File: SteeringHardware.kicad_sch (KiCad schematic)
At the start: 59 parts, among them J1 Conn_ARM_JTAG_SWD_10, J10 Output, J11 Input, J12 Output, J13 Input, J14 Input, J15 Output, J16 Input, J17 Output, J18 Output, J19 Input, J2 USB_B_Micro, J20 Input, J3 Conn_01x09_Female, J4 Output, J5 Input, J6 Input, J7 Output, J8 Input, J9 Input, Q1 AO3400A, Q2 AO3400A, Q3 AO3400A, Q4 AO3400A, Q5 AO3400A, Q6 AO3400A, Q7 AO3400A, U1 STM32F072RBTx, U3 TPS2113, U4 TCAN1042xV, U6 TPS5430DDA, U7 HY28B

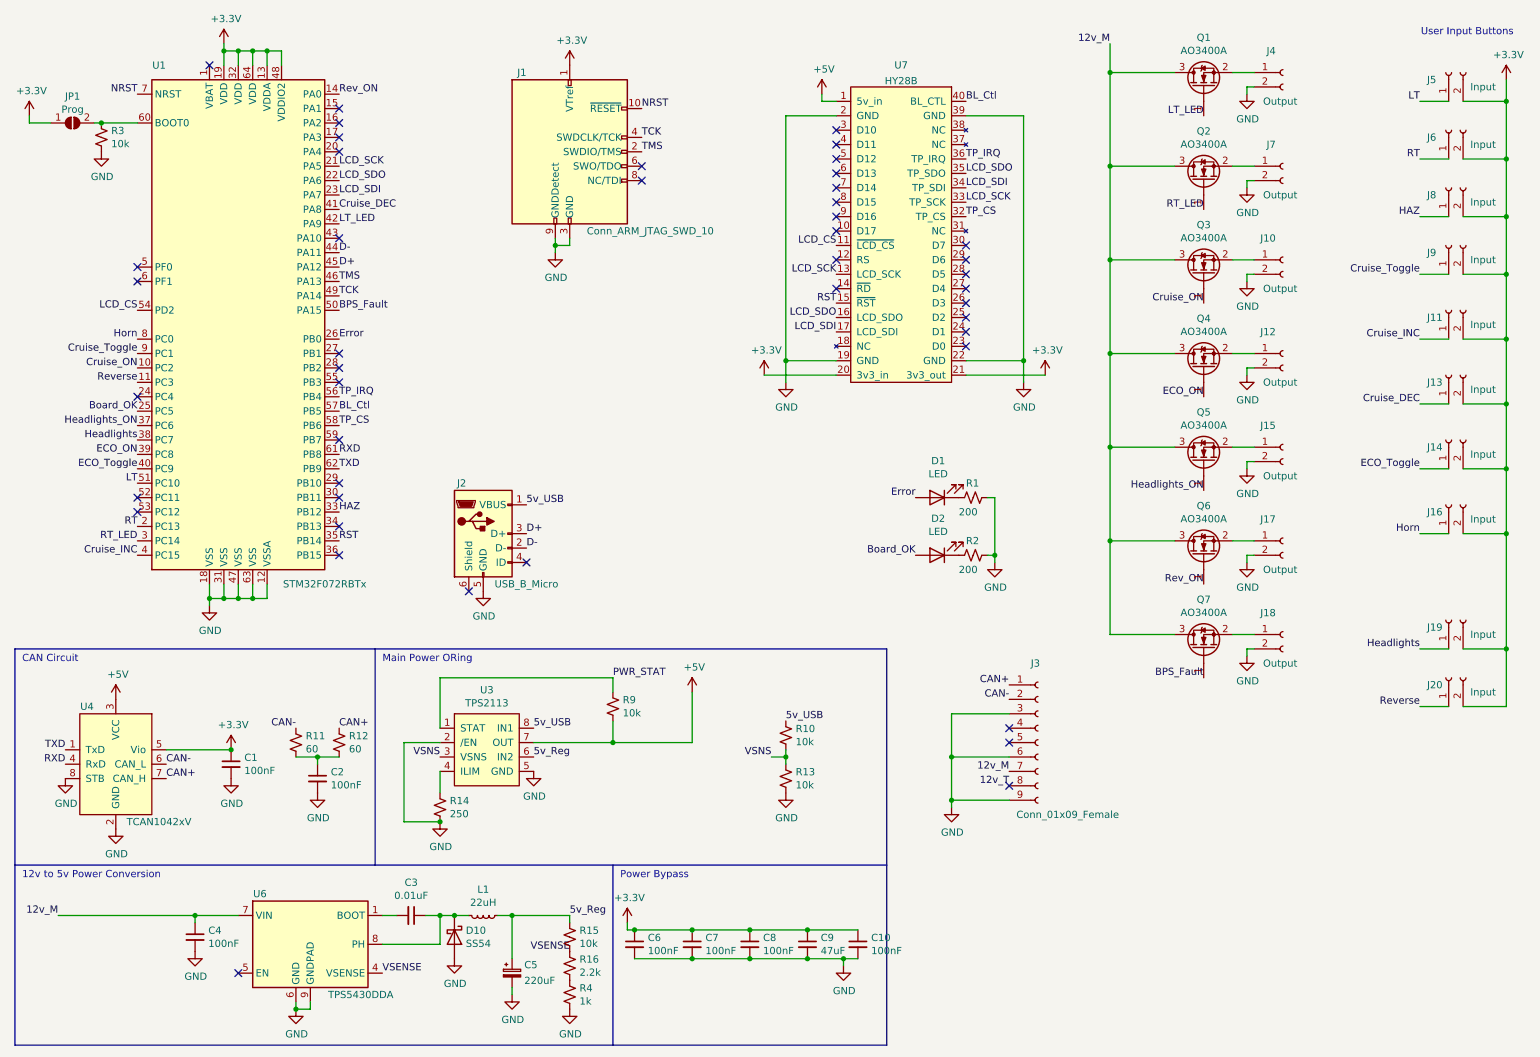
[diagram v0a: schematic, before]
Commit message: Fixed LED Fets
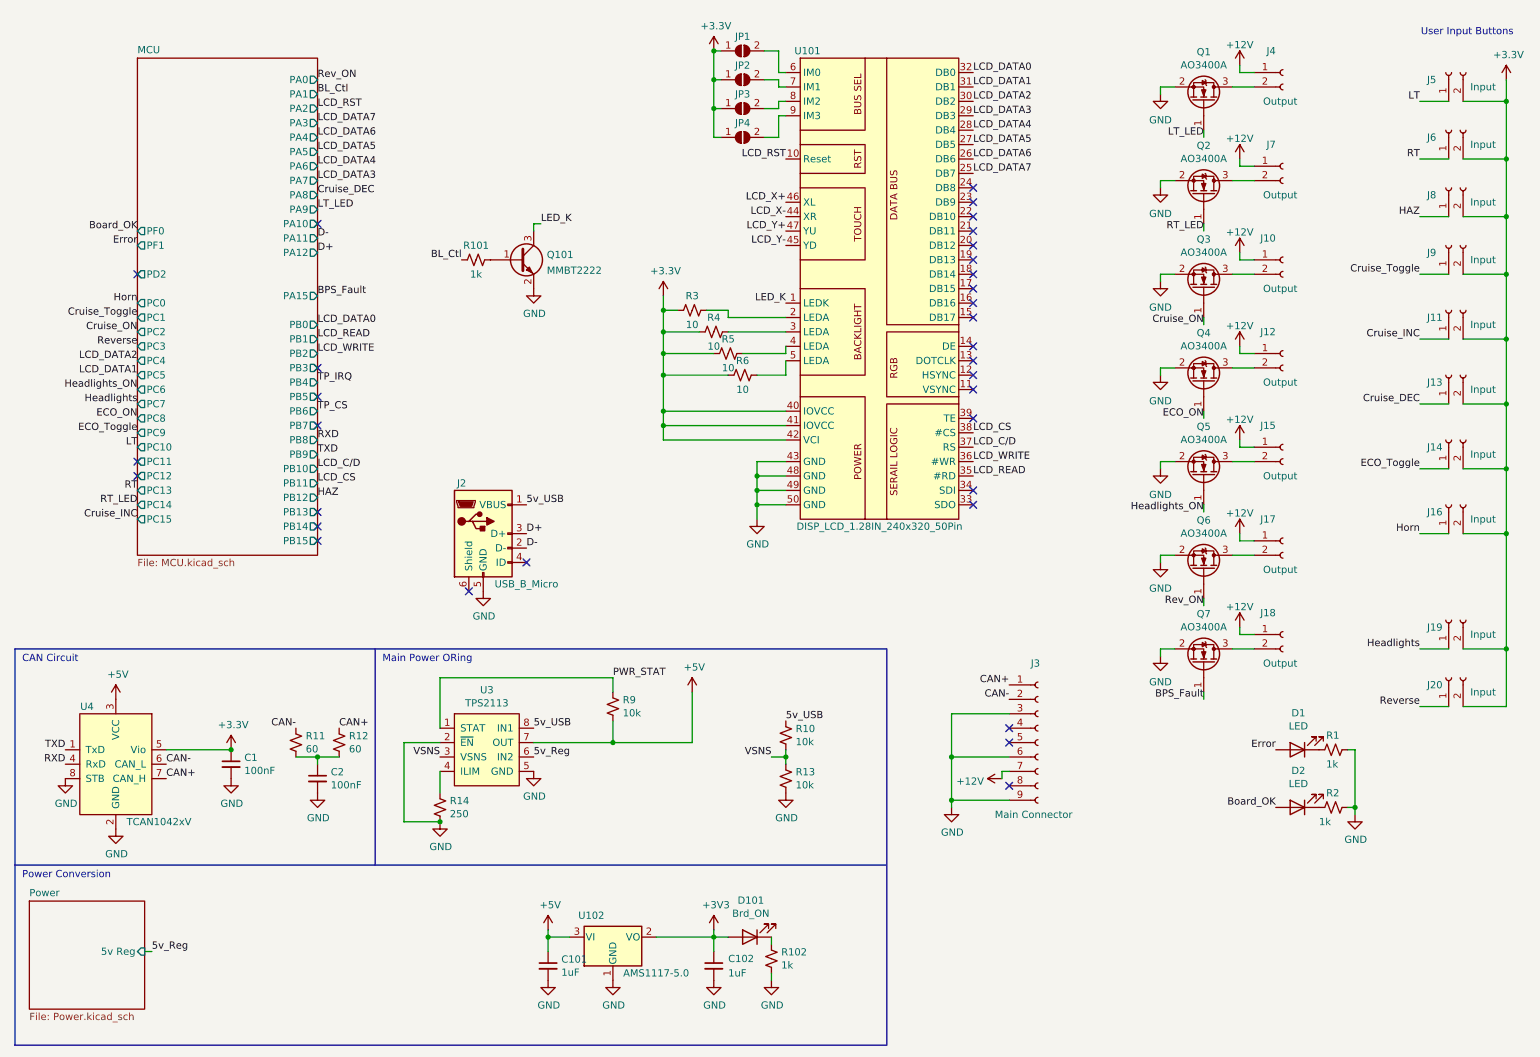
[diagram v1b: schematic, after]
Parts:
- removed C10, C4, C6, C7, C8: 100nF, Capacitor_SMD:C_0402_1005Metric, symbol Device:C_Small
- removed C3: 0.01uF, Capacitor_SMD:C_0402_1005Metric, symbol Device:C_Small
- removed C5: 220uF, Capacitor_SMD:CP_Elec_8x5.4, symbol Device:C_Polarized_Small
- removed C9: 47uF, Capacitor_SMD:C_0805_2012Metric, symbol Device:C_Small
- removed D10: SS54, Diode_SMD:D_SOD-123, symbol Diode:B340
- removed J1: Conn_ARM_JTAG_SWD_10, Connector_PinHeader_1.27mm:PinHeader_2x05_P1.27mm_Vertical_SMD, symbol Connector:Conn_ARM_JTAG_SWD_10
- removed L1: 22uH, JohnLib:L_Panasonic_YFP, symbol Device:L_Small
- removed R15: 10k, Resistor_SMD:R_0603_1608Metric, symbol Device:R_Small_US
- removed R16: 2.2k, Resistor_SMD:R_0603_1608Metric, symbol Device:R_Small_US
- removed U1: STM32F072RBTx, Package_QFP:LQFP-64_10x10mm_P0.5mm, symbol MCU_ST_STM32F0:STM32F072RBTx
- removed U6: TPS5430DDA, Package_SO:TI_SO-PowerPAD-8_ThermalVias, symbol Regulator_Switching:TPS5430DDA
- removed U7: HY28B, JohnLib:HY28B, symbol JohnLib:HY28B
- added C101, C102: 1uF, Capacitor_SMD:C_0402_1005Metric, symbol Device:C_Small
- added D101: Brd_ON, LED_SMD:LED_0805_2012Metric, symbol Device:LED
- added JP2, JP3, JP4: SolderJumper_2_Open, Jumper:SolderJumper-2_P1.3mm_Open_RoundedPad1.0x1.5mm, symbol Jumper:SolderJumper_2_Open
- added Q101: MMBT2222, Package_TO_SOT_SMD:SOT-23, symbol Device:Q_NPN_BEC
- added R101, R102: 1k, Resistor_SMD:R_0603_1608Metric, symbol Device:R_Small_US
- added R5, R6: 10, Resistor_SMD:R_0603_1608Metric, symbol Device:R_Small_US
- added U101: DISP_LCD_1.28IN_240x320_50Pin, Connector_FFC-FPC:Molex_54132-5033_1x50-1MP_P0.5mm_Horizontal, symbol JohnLib:DISP_LCD_1.28IN_240x320_50Pin
- added U102: AMS1117-5.0, Package_TO_SOT_SMD:SOT-223-3_TabPin2, symbol Regulator_Linear:AMS1117-5.0
- J3: value Conn_01x09_Female -> Main Connector
- JP1: value Prog -> SolderJumper_2_Open; footprint Connector_PinHeader_2.54mm:PinHeader_1x02_P2.54mm_Vertical -> Jumper:SolderJumper-2_P1.3mm_Open_RoundedPad1.0x1.5mm
- R1, R2: value 200 -> 1k; LCSC Part C8218 -> C21190
- R3: value 10k -> 10; LCSC Part C25804 -> C22859
- R4: value 1k -> 10; LCSC Part C21190 -> C22859
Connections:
- net +3V3: now also R3.1, R4.1, C102.1, D101.2 (A), JP2.1 (A), JP3.1 (A), JP4.1 (A), R5.1, R6.1, U101.40 (IOVCC), U101.41 (IOVCC), U101.42 (VCI), U102.2 (VO)
- net +5V: now also C101.1, U102.3 (VI)
- net BL_Ctl: now also R101.1
- net GND: now also Q1.2 (S), Q2.2 (S), Q3.2 (S), Q4.2 (S), Q5.2 (S), Q6.2 (S), Q7.2 (S), C101.2, C102.2, Q101.2 (E), R102.2, U101.43 (GND), U101.48 (GND), U101.49 (GND), U101.50 (GND), U102.1 (GND); no longer J10.2 (Pin_2), J12.2 (Pin_2), J15.2 (Pin_2), J17.2 (Pin_2), J18.2 (Pin_2), J4.2 (Pin_2), J7.2 (Pin_2), R3.2, R4.2
- net LCD_CS: now also U101.38 (#CS)
- net at JP1.2 (B): now also U101.6 (IM0); no longer R3.1
- net +12V: now reaches J4.1 (Pin_1)
- net +12V: now also J10.1 (Pin_1), J12.1 (Pin_1), J15.1 (Pin_1), J17.1 (Pin_1), J18.1 (Pin_1), J3.7 (Pin_7), J7.1 (Pin_1); no longer Q1.2 (S)
- removed net 12v_M: J3.7 (Pin_7), Q1.3 (D), Q2.3 (D), Q3.3 (D), Q4.3 (D), Q5.3 (D), Q6.3 (D), Q7.3 (D)
- net 12v_T: no longer names the net of J3.8 (Pin_8)
- new net: J4.2 (Pin_2), Q1.3 (D)
- new net: J7.2 (Pin_2), Q2.3 (D)
- new net: J10.2 (Pin_2), Q3.3 (D)
- new net: J12.2 (Pin_2), Q4.3 (D)
- new net: J15.2 (Pin_2), Q5.3 (D)
- new net: J17.2 (Pin_2), Q6.3 (D)
- new net: J18.2 (Pin_2), Q7.3 (D)
- new net: Q101.1 (B), R101.2
- new net: JP2.2 (B), U101.7 (IM1)
- new net: D101.1 (K), R102.1
- new net: R5.2, U101.4 (LEDA)
- new net: JP3.2 (B), U101.8 (IM2)
- new net: JP4.2 (B), U101.9 (IM3)
- new net: R4.2, U101.3 (LEDA)
- new net: R3.2, U101.2 (LEDA)
- new net: R6.2, U101.5 (LEDA)
- new net LCD_C/D: U101.37 (RS)
- new net LCD_DATA0: U101.32 (DB0)
- new net LCD_DATA1: U101.31 (DB1)
- new net LCD_DATA2: U101.30 (DB2)
- new net LCD_DATA3: U101.29 (DB3)
- new net LCD_DATA4: U101.28 (DB4)
- new net LCD_DATA5: U101.27 (DB5)
- new net LCD_DATA6: U101.26 (DB6)
- new net LCD_DATA7: U101.25 (DB7)
- new net LCD_READ: U101.35 (#RD)
- new net LCD_RST: U101.10 (Reset)
- new net LCD_WRITE: U101.36 (#WR)
- new net LCD_X+: U101.46 (XL)
- new net LCD_X-: U101.44 (XR)
- new net LCD_Y+: U101.47 (YU)
- new net LCD_Y-: U101.45 (YD)
- new net LED_K: Q101.3 (C), U101.1 (LEDK)
- no-connect marks 45 -> 32
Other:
- added sheet MCU (MCU.kicad_sch)
- added sheet Power (Power.kicad_sch)
- note added: "Power Conversion"
- note removed: "12v to 5v Power Conversion"
- note removed: "Power Bypass"
- moved on the sheet: D1, D2, Q1, Q2, Q3, Q4, Q5, Q6, Q7, R1, R2

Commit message: Current board
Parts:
- removed J10, J12, J15, J17, J18, J4, J7: Output, Connector_Molex:Molex_Micro-Fit_3.0_43650-0215_1x02_P3.00mm_Vertical, symbol Connector:Conn_01x02_Female
- removed J11, J13, J14, J16, J19, J20, J5, J6, J8, J9: Input, Connector_Molex:Molex_Micro-Fit_3.0_43650-0215_1x02_P3.00mm_Vertical, symbol Connector:Conn_01x02_Female
- removed R12: 60, Resistor_SMD:R_0603_1608Metric, symbol Device:R_Small_US
- added J101: Conn1, JohnLib:Connector_FPC_Molex_2004850410, symbol Connector_Generic_MountingPin:Conn_01x10_MountingPin
- added J102: Conn2, JohnLib:Connector_FPC_Molex_2004850410, symbol Connector_Generic_MountingPin:Conn_01x10_MountingPin
- added J103: RT_LED, Connector_Molex:Molex_Micro-Fit_3.0_43650-0215_1x02_P3.00mm_Vertical, symbol Connector:Conn_01x02_Female
- added J104: RT_BTN, Connector_Molex:Molex_Micro-Fit_3.0_43650-0215_1x02_P3.00mm_Vertical, symbol Connector:Conn_01x02_Female
- added J105: LT_LED, Connector_Molex:Molex_Micro-Fit_3.0_43650-0215_1x02_P3.00mm_Vertical, symbol Connector:Conn_01x02_Female
- added J106: LT_BTN, Connector_Molex:Molex_Micro-Fit_3.0_43650-0215_1x02_P3.00mm_Vertical, symbol Connector:Conn_01x02_Female
- R11: value 60 -> 120; footprint Resistor_SMD:R_0603_1608Metric -> Resistor_SMD:R_1206_3216Metric; LCSC Part (none) -> C17909
- U102: LCSC Part C347222 -> C6186
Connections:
- net +12V: now also J101.10 (Pin_10), J102.10 (Pin_10), J103.1 (Pin_1), J105.1 (Pin_1)
- net +5V: now also C2.1
- net BPS_Fault: now also Q7.3 (D); no longer Q7.1 (G)
- net CAN+: now also R11.2
- net Cruise_DEC: now also J102.4 (Pin_4)
- net Cruise_INC: now also J101.6 (Pin_6)
- net Cruise_ON: now also Q3.3 (D), J102.3 (Pin_3); no longer Q3.1 (G)
- net Cruise_Toggle: now also J102.2 (Pin_2)
- net ECO_ON: now also Q4.3 (D), J101.3 (Pin_3); no longer Q4.1 (G)
- net ECO_Toggle: now also J101.2 (Pin_2)
- net GND: now also J101.1 (Pin_1), J102.1 (Pin_1), J104.2 (Pin_2), J106.2 (Pin_2)
- net HAZ: now also J102.6 (Pin_6)
- net Headlights: now also J101.4 (Pin_4)
- net Headlights_ON: now also Q5.3 (D), J101.5 (Pin_5); no longer Q5.1 (G)
- net Horn: now also J101.8 (Pin_8)
- net LT: now also J106.1 (Pin_1)
- net LT_LED: now also Q1.3 (D), J105.2 (Pin_2); no longer Q1.1 (G)
- net RT: now also J104.1 (Pin_1)
- net RT_LED: now also Q2.3 (D), J103.2 (Pin_2); no longer Q2.1 (G)
- net Rev_ON: now also Q6.3 (D), J102.9 (Pin_9); no longer Q6.1 (G)
- net Reverse: now also J102.8 (Pin_8)
- new net BPS_Fault_EN: Q7.1 (G)
- new net Cruise_ON_EN: Q3.1 (G)
- new net ECO_ON_EN: Q4.1 (G)
- new net Headlights_ON_EN: Q5.1 (G)
- new net LT_LED_EN: Q1.1 (G)
- new net RT_LED_EN: Q2.1 (G)
- new net Rev_ON_EN: Q6.1 (G)
- no-connect marks 32 -> 38
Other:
- note removed: "User Input Buttons"
- moved on the sheet: C2, D1, D2, Q1, Q2, Q3, Q4, Q5, Q6, Q7, R1, R11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

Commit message: Rename LCSC Field
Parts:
- C1, C2: LCSC Part C307331 -> (none); LCSC# (none) -> C307331
- C101, C102: LCSC Part C52923 -> (none); LCSC# (none) -> C52923
- D1: LCSC Part C84256 -> (none); LCSC# (none) -> C84256
- D101: LCSC Part C2297 -> (none); LCSC# (none) -> C2297
- D2: LCSC Part C72043 -> (none); LCSC# (none) -> C72043
- Q1, Q2, Q3, Q4, Q5, Q6, Q7: LCSC Part C20917 -> (none); LCSC# (none) -> C20917
- Q101: LCSC Part C8512 -> (none); LCSC# (none) -> C8512
- R1, R101, R102, R2: LCSC Part C21190 -> (none); LCSC# (none) -> C21190
- R10, R13, R9: LCSC Part C25804 -> (none); LCSC# (none) -> C25804
- R11: LCSC Part C17909 -> (none); LCSC# (none) -> C17909
- R14: LCSC Part C22962 -> (none); LCSC# (none) -> C22962
- R3, R4, R5, R6: LCSC Part C22859 -> (none); LCSC# (none) -> C22859
- U102: LCSC Part C6186 -> (none); LCSC# (none) -> C6186
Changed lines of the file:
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@@
       (effects (font (size 1.27 1.27)) hide)
     )
-    (property "LCSC Part" "C307331" (id 4) (at 52.07 146.05 0)
+    (property "LCSC#" "C307331" (id 4) (at 52.07 146.05 0)
       (effects (font (size 1.27 1.27)) hide)
     )
@@
       (effects (font (size 1.27 1.27)) hide)
     )
-    (property "LCSC Part" "C307331" (id 4) (at 36.83 133.35 0)
+    (property "LCSC#" "C307331" (id 4) (at 36.83 133.35 0)
       (effects (font (size 1.27 1.27)) hide)
     )
@@
       (effects (font (size 1.27 1.27)) hide)
     )
-    (property "LCSC Part" "C17909" (id 4) (at 66.04 133.35 90)
+    (property "LCSC#" "C17909" (id 4) (at 66.04 133.35 90)
       (effects (font (size 1.27 1.27)) hide)
     )
@@
       (effects (font (size 1.27 1.27)) hide)
     )
-    (property "LCSC Part" "C22962" (id 4) (at 88.9 153.67 0)
+    (property "LCSC#" "C22962" (id 4) (at 88.9 153.67 0)
       (effects (font (size 1.27 1.27)) hide)
     )
@@
       (effects (font (size 1.27 1.27)) hide)
     )
-    (property "LCSC Part" "C25804" (id 4) (at 119.38 135.89 0)
+    (property "LCSC#" "C25804" (id 4) (at 119.38 135.89 0)
       (effects (font (size 1.27 1.27)) hide)
     )
@@
       (effects (font (size 1.27 1.27)) hide)
     )
-    (property "LCSC Part" "C25804" (id 4) (at 149.86 140.97 0)
+    (property "LCSC#" "C25804" (id 4) (at 149.86 140.97 0)
       (effects (font (size 1.27 1.27)) hide)
     )
@@
       (effects (font (size 1.27 1.27)) hide)
     )
-    (property "LCSC Part" "C25804" (id 4) (at 149.86 148.59 0)
+    (property "LCSC#" "C25804" (id 4) (at 149.86 148.59 0)
       (effects (font (size 1.27 1.27)) hide)
     )
@@
       (effects (font (size 1.27 1.27)) hide)
     )
-    (property "LCSC Part" "C20917" (id 4) (at 217.17 22.86 90)
+    (property "LCSC#" "C20917" (id 4) (at 217.17 22.86 90)
       (effects (font (size 1.27 1.27)) hide)
     )
@@
       (effects (font (size 1.27 1.27)) hide)
     )
-    (property "LCSC Part" "C20917" (id 4) (at 237.49 22.86 90)
+    (property "LCSC#" "C20917" (id 4) (at 237.49 22.86 90)
       (effects (font (size 1.27 1.27)) hide)
     )
@@
       (effects (font (size 1.27 1.27)) hide)
     )
-    (property "LCSC Part" "C20917" (id 4) (at 217.17 41.91 90)
+    (property "LCSC#" "C20917" (id 4) (at 217.17 41.91 90)
       (effects (font (size 1.27 1.27)) hide)
     )
@@
       (effects (font (size 1.27 1.27)) hide)
     )
-    (property "LCSC Part" "C20917" (id 4) (at 238.76 41.91 90)
+    (property "LCSC#" "C20917" (id 4) (at 238.76 41.91 90)
       (effects (font (size 1.27 1.27)) hide)
     )
@@
       (effects (font (size 1.27 1.27)) hide)
     )
-    (property "LCSC Part" "C20917" (id 4) (at 217.17 60.96 90)
+    (property "LCSC#" "C20917" (id 4) (at 217.17 60.96 90)
       (effects (font (size 1.27 1.27)) hide)
     )
@@
       (effects (font (size 1.27 1.27)) hide)
     )
-    (property "LCSC Part" "C20917" (id 4) (at 238.76 60.96 90)
+    (property "LCSC#" "C20917" (id 4) (at 238.76 60.96 90)
       (effects (font (size 1.27 1.27)) hide)
     )
@@
       (effects (font (size 1.27 1.27)) hide)
     )
-    (property "LCSC Part" "C20917" (id 4) (at 217.17 80.01 90)
+    (property "LCSC#" "C20917" (id 4) (at 217.17 80.01 90)
       (effects (font (size 1.27 1.27)) hide)
     )
@@
       (effects (font (size 1.27 1.27)) hide)
     )
-    (property "LCSC Part" "C84256" (id 4) (at 212.09 138.43 0)
+    (property "LCSC#" "C84256" (id 4) (at 212.09 138.43 0)
       (effects (font (size 1.27 1.27)) hide)
     )
@@
       (effects (font (size 1.27 1.27)) hide)
     )
-    (property "LCSC Part" "C72043" (id 4) (at 212.09 148.59 0)
+    (property "LCSC#" "C72043" (id 4) (at 212.09 148.59 0)
       (effects (font (size 1.27 1.27)) hide)
     )
@@
       (effects (font (size 1.27 1.27)) hide)
     )
-    (property "LCSC Part" "C21190" (id 4) (at 218.44 138.43 90)
+    (property "LCSC#" "C21190" (id 4) (at 218.44 138.43 90)
       (effects (font (size 1.27 1.27)) hide)
     )
@@
       (effects (font (size 1.27 1.27)) hide)
     )
-    (property "LCSC Part" "C21190" (id 4) (at 218.44 148.59 90)
+    (property "LCSC#" "C21190" (id 4) (at 218.44 148.59 90)
       (effects (font (size 1.27 1.27)) hide)
     )
@@
       (effects (font (size 1.27 1.27)) hide)
     )
-    (property "LCSC Part" "C21190" (id 4) (at 95.25 57.15 90)
+    (property "LCSC#" "C21190" (id 4) (at 95.25 57.15 90)
       (effects (font (size 1.27 1.27)) hide)
     )
@@
       (effects (font (size 1.27 1.27)) hide)
     )
-    (property "LCSC Part" "C21190" (id 4) (at 147.32 180.34 0)
+    (property "LCSC#" "C21190" (id 4) (at 147.32 180.34 0)
       (effects (font (size 1.27 1.27)) hide)
     )
@@
       (effects (font (size 1.27 1.27)) hide)
     )
-    (property "LCSC Part" "C22859" (id 4) (at 139.7 73.66 90)
+    (property "LCSC#" "C22859" (id 4) (at 139.7 73.66 90)
       (effects (font (size 1.27 1.27)) hide)
     )
@@
       (effects (font (size 1.27 1.27)) hide)
     )
-    (property "LCSC Part" "C52923" (id 4) (at 107.95 181.61 0)
+    (property "LCSC#" "C52923" (id 4) (at 107.95 181.61 0)
       (effects (font (size 1.27 1.27)) hide)
     )
@@
       (effects (font (size 1.27 1.27)) hide)
     )
-    (property "LCSC Part" "C52923" (id 4) (at 137.16 181.61 0)
+    (property "LCSC#" "C52923" (id 4) (at 137.16 181.61 0)
       (effects (font (size 1.27 1.27)) hide)
     )
@@
       (effects (font (size 1.27 1.27)) hide)
     )
-    (property "LCSC Part" "C2297" (id 4) (at 143.51 176.53 0)
+    (property "LCSC#" "C2297" (id 4) (at 143.51 176.53 0)
       (effects (font (size 1.27 1.27)) hide)
     )
@@
       (effects (font (size 1.27 1.27)) hide)
     )
-    (property "LCSC Part" "C8512" (id 4) (at 102.87 57.15 0)
+    (property "LCSC#" "C8512" (id 4) (at 102.87 57.15 0)
       (effects (font (size 1.27 1.27)) hide)
     )
@@
       (effects (font (size 1.27 1.27)) hide)
     )
-    (property "LCSC Part" "C22859" (id 4) (at 137.16 69.85 90)
+    (property "LCSC#" "C22859" (id 4) (at 137.16 69.85 90)
       (effects (font (size 1.27 1.27)) hide)
     )
@@
       (effects (font (size 1.27 1.27)) hide)
     )
-    (property "LCSC Part" "C6186" (id 4) (at 119.38 176.53 0)
+    (property "LCSC#" "C6186" (id 4) (at 119.38 176.53 0)
       (effects (font (size 1.27 1.27)) hide)
     )
@@
       (effects (font (size 1.27 1.27)) hide)
     )
-    (property "LCSC Part" "C22859" (id 4) (at 133.35 66.04 90)
+    (property "LCSC#" "C22859" (id 4) (at 133.35 66.04 90)
       (effects (font (size 1.27 1.27)) hide)
     )
@@
       (effects (font (size 1.27 1.27)) hide)
     )
-    (property "LCSC Part" "C22859" (id 4) (at 142.24 77.47 90)
-      (effects (font (size 1.27 1.27)) hide)
-    )
+    (property "LCSC#" "C22859" (id 4) (at 142.24 77.47 90)
+      (effects (font (size 1.27 1.27)) hide)
+    )
